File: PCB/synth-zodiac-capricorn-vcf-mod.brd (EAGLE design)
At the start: 76.1 x 72.4 mm, 14 parts, among them U1 TL072A

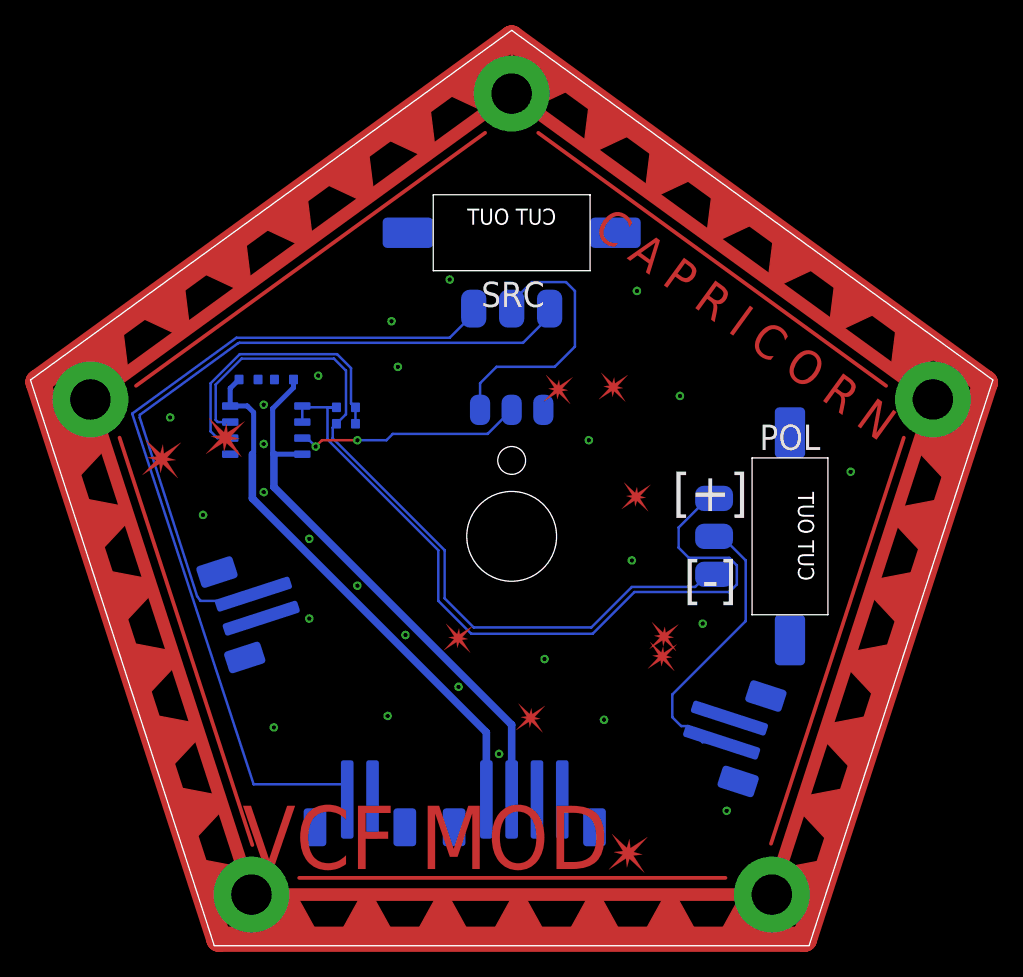
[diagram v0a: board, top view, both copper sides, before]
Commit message: Almost ready for FAB.
Sagittarius was mis-spelled, renamed it.  Taurus is still WIP.
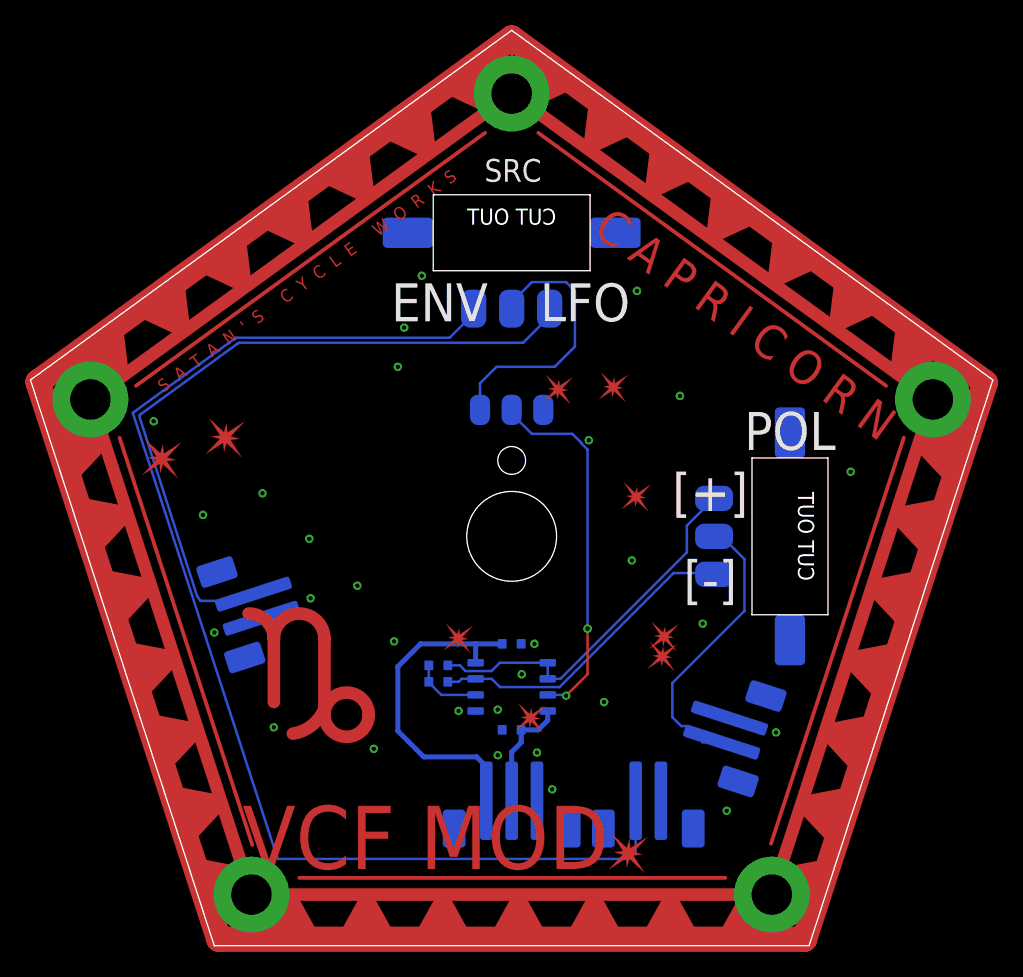
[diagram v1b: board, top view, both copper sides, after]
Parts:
- removed C41, C42: 0.1uF, rlc:0603-CAP
- removed EG: 2-pin, VT, SMT, con-jst:B2B-PH-SM4
- removed J4: (no value), con-jst:B4B-PH-SM4
- removed R72, R73: 10.0K, rlc:0603-RES
- added C1, C2: 0.1uF, rlc:0603-CAP
- added EG_IN: 2-pin, VT, SMT, con-jst:B2B-PH-SM4
- added GLYPH1: Capricorn, circuit-monkey-zodiac:CAPRICORN-GLYPH
- added PWR: JST, 3P, VT, SMT, con-jst:B3B-PH-SM4
- added R1, R2: 10.0K, rlc:0603-RES
- moved U1 28.1 mm to (38.0, 21.1)
- renumbered LFO to LFO_IN, VCF_OUT to MOD2VCF
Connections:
- net +9V: now also C1.1, PWR.1; no longer C41.1, J4.1
- net -9V: now also C2.2, PWR.2; no longer C42.2, J4.2
- net EG: now also EG_IN.1; no longer EG.1
- net GND: now also C1.2, C2.1, EG_IN.2, PWR.3; no longer C41.2, C42.1, EG.2, J4.4
- net MOD_N: now also R2.2; no longer R72.2
- net MOD_P: now also R1.1; no longer R73.1
- net N$99: now also R1.2, R2.1; no longer R72.1, R73.2
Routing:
- net MOD_N: track 61.7 -> 25.2 mm
- net -9V: track 44.0 -> 9.07 mm
- net MOD_P: track 62.0 -> 29.9 mm
- net EG: track 69.5 -> 99.7 mm
- net N$99: track 22.7 -> 5.46 mm
- net +9V: track 42.7 -> 26.4 mm
- net AMT: track 18.0 -> 29.1 mm
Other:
- board text added: "ENV"
- board text added: "LFO"
- board text added: "Rev. A"

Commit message: Work in progress for rev A,  VCO rev.B
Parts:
- EG_IN, LFO_IN, MOD2VCF: value 2-pin, VT, SMT -> JST, SH, 2P; device con-jst:B2B-PH-SM4 -> con-jst:BM02B-SRSS-TB
- POL, SRC: value SPDT -> (none)
- PWR: value JST, 3P, VT, SMT -> JST SM 3P; device con-jst:B3B-PH-SM4 -> con-jst:BM03B-SRSS-TB
- moved PWR 13.4 mm to (24.7, 11.7)
- moved LFO_IN 7.82 mm to (15.3, 34.6)
- moved C2 6.56 mm to (34.0, 12.5)
- moved U1 6.34 mm to (34.1, 16.1)
- moved C1 6.26 mm to (34.1, 19.6)
- moved R1 5.56 mm to (28.8, 18.4)
- moved R2 5.56 mm to (28.8, 17.1)
- moved EG_IN 4.66 mm to (53.1, 11.7)
- moved MOD2VCF 2.08 mm to (55.3, 18.2)
- moved SRC 1.20 mm to (38.0, 55.8)
- moved AMT 0.91 mm to (37.9, 32.1)
- moved POL 0.10 mm to (59.9, 33.0)
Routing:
- net MOD_SRC: track 21.7 -> 8.78 mm
- net AMT: track 29.1 -> 41.4 mm
- net -9V: track 9.07 -> 20.2 mm
- net LFO_CV: track 55.6 -> 45.3 mm
- net MOD_N: track 25.2 -> 34.5 mm
- net +9V: track 26.4 -> 18.3 mm, vias 0 -> 2
- net MOD_P: track 29.9 -> 37.2 mm
- net VCF_MOD: track 22.8 -> 17.2 mm
- net EG: track 99.7 -> 102.4 mm
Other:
- board text added: "+"
- board text added: "-"
- board text removed: "[+]"
- board text removed: "[-]"

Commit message: Perhaps final Rev. A?
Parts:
- POL, SRC: device switch-thd:SS-12-F45-PNL-SMT -> switch-thd:SS-12-F45-PNL-SMT-2
- flipped POL to the top, turned to 270 degrees
- flipped SRC to the top
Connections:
- net EG: now also SRC.A; no longer SRC.B
- net GND: now also POL.MTG3, POL.MTG4, SRC.MTG3, SRC.MTG4
- net LFO_CV: now also SRC.B; no longer SRC.A
- net MOD_N: now also POL.B; no longer POL.A
- net MOD_P: now also POL.A; no longer POL.B
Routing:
- net EG: track 102.4 -> 104.2 mm
- net LFO_CV: track 45.3 -> 44.2 mm
- net MOD_N: track 34.5 -> 35.6 mm
- net MOD_P: track 37.2 -> 38.2 mm
- net MOD_SRC: track 8.78 -> 9.68 mm
